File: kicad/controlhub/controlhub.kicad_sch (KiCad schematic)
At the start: 0 parts

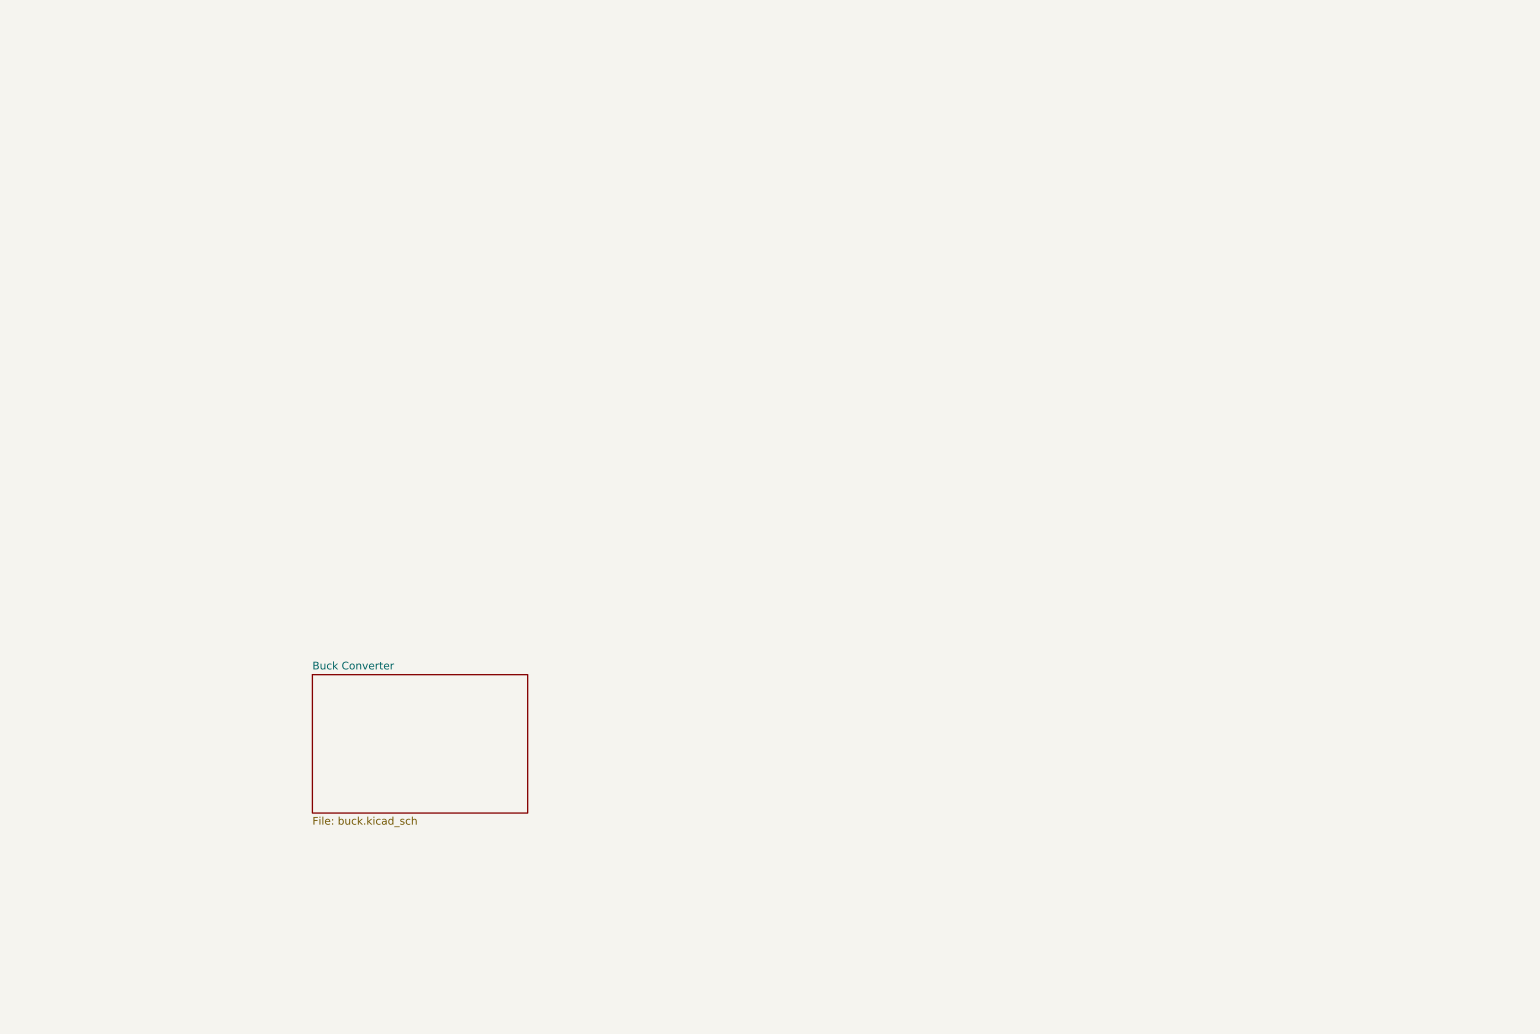
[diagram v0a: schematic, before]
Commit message: added converter and started servo driver
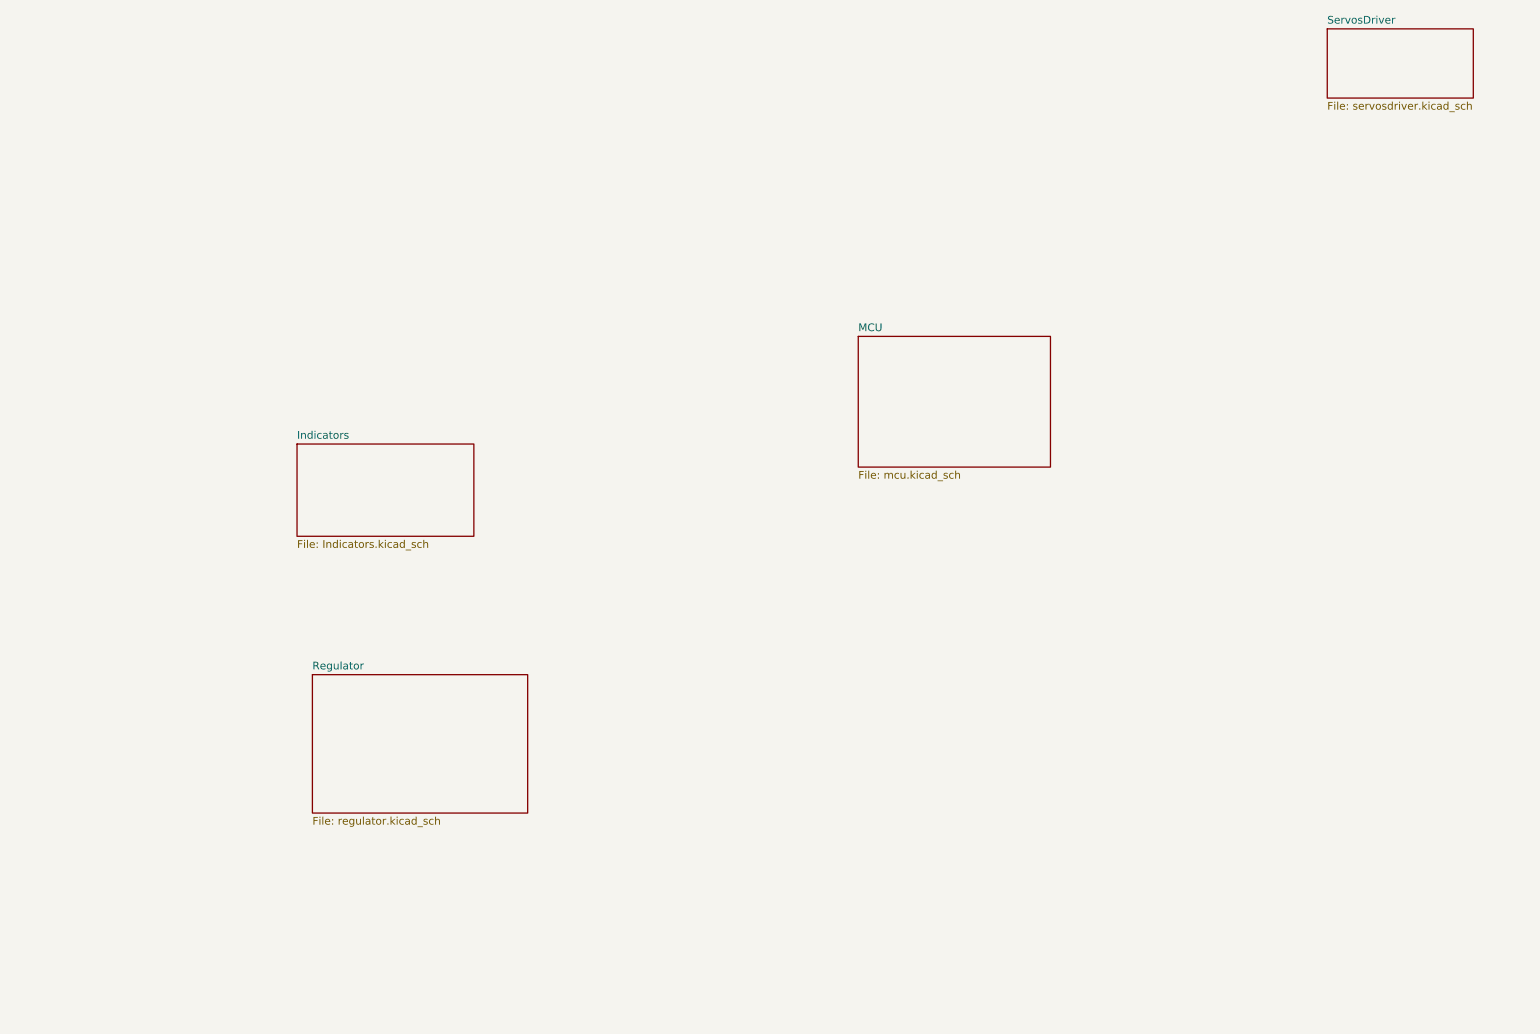
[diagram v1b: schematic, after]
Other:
- sheet Buck Converter renamed Regulator
- added sheet Indicators (Indicators.kicad_sch)
- added sheet MCU (mcu.kicad_sch)
- added sheet ServosDriver (servosdriver.kicad_sch)
- sheet Regulator: file buck.kicad_sch -> regulator.kicad_sch
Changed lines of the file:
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@@
+	)
+	(sheet
+		(at 63.5 102.87)
+		(size 29.21 15.24)
+		(exclude_from_sim no)
+		(in_bom yes)
+		(on_board yes)
+		(dnp no)
+		(fields_autoplaced yes)
+		(stroke
+			(width 0.1524)
+			(type solid)
+		)
+		(fill
+			(color 0 0 0 0.0000)
+		)
+		(property "Sheetname" "Indicators"
+			(at 63.5 102.1584 0)
+			(effects
+				(font
+					(size 1.27 1.27)
+				)
+				(justify left bottom)
+			)
+		)
+		(property "Sheetfile" "Indicators.kicad_sch"
+			(at 63.5 118.6946 0)
+			(effects
+				(font
+					(size 1.27 1.27)
+				)
+				(justify left top)
+			)
+		)
+		(instances
+			(project "controlhub"
+				(path "/78f9b8b9-94ed-46bb-ab2b-797c156bf665"
+					(page "3")
+				)
+			)
+		)
+	)
+	(sheet
+		(at 156.21 85.09)
+		(size 31.75 21.59)
+		(exclude_from_sim no)
+		(in_bom yes)
+		(on_board yes)
+		(dnp no)
+		(fields_autoplaced yes)
+		(stroke
+			(width 0.1524)
+			(type solid)
+		)
+		(fill
+			(color 0 0 0 0.0000)
+		)
+		(property "Sheetname" "MCU"
+			(at 156.21 84.3784 0)
+			(effects
+				(font
+					(size 1.27 1.27)
+				)
+				(justify left bottom)
+			)
+		)
+		(property "Sheetfile" "mcu.kicad_sch"
+			(at 156.21 107.2646 0)
+			(effects
+				(font
+					(size 1.27 1.27)
+				)
+				(justify left top)
+			)
+		)
+		(instances
+			(project "controlhub"
+				(path "/78f9b8b9-94ed-46bb-ab2b-797c156bf665"
+					(page "4")
+				)
+			)
+		)
 	)
 	(sheet
@@
 			(color 0 0 0 0.0000)
 		)
-		(property "Sheetname" "Buck Converter"
+		(property "Sheetname" "Regulator"
 			(at 66.04 140.2584 0)
 			(effects
@@
 			)
 		)
-		(property "Sheetfile" "buck.kicad_sch"
+		(property "Sheetfile" "regulator.kicad_sch"
 			(at 66.04 164.4146 0)
 			(effects
@@
 				)
 			)
+		)
+	)
+	(sheet
+		(at 233.68 34.29)
+		(size 24.13 11.43)
+		(exclude_from_sim no)
+		(in_bom yes)
+		(on_board yes)
+		(dnp no)
+		(fields_autoplaced yes)
+		(stroke
+			(width 0.1524)
+			(type solid)
+		)
+		(fill
+			(color 0 0 0 0.0000)
+		)
+		(property "Sheetname" "ServosDriver"
+			(at 233.68 33.5784 0)
+			(effects
+				(font
+					(size 1.27 1.27)
+				)
+				(justify left bottom)
+			)
+		)
+		(property "Sheetfile" "servosdriver.kicad_sch"
+			(at 233.68 46.3046 0)
+			(effects
+				(font
+					(size 1.27 1.27)
+				)
+				(justify left top)
+			)
+		)
+		(instances
+			(project "controlhub"
+				(path "/78f9b8b9-94ed-46bb-ab2b-797c156bf665"
+					(page "5")
+				)
+			)

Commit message: added driver
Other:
- added sheet MotorDriver (motordriver.kicad_sch)
- added sheet MotorDriver1 (motordriver.kicad_sch)
- added sheet MotorDriver2 (motordriver.kicad_sch)
- added sheet MotorDriver3 (motordriver.kicad_sch)
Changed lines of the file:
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@@
+	)
+	(sheet
+		(at 77.47 41.91)
+		(size 26.67 15.24)
+		(exclude_from_sim no)
+		(in_bom yes)
+		(on_board yes)
+		(dnp no)
+		(fields_autoplaced yes)
+		(stroke
+			(width 0.1524)
+			(type solid)
+		)
+		(fill
+			(color 0 0 0 0.0000)
+		)
+		(property "Sheetname" "MotorDriver"
+			(at 77.47 41.1984 0)
+			(effects
+				(font
+					(size 1.27 1.27)
+				)
+				(justify left bottom)
+			)
+		)
+		(property "Sheetfile" "motordriver.kicad_sch"
+			(at 77.47 57.7346 0)
+			(effects
+				(font
+					(size 1.27 1.27)
+				)
+				(justify left top)
+			)
+		)
+		(instances
+			(project "controlhub"
+				(path "/78f9b8b9-94ed-46bb-ab2b-797c156bf665"
+					(page "6")
+				)
+			)
+		)
 	)
 	(sheet
@@
 	)
 	(sheet
-		(at 66.04 140.97)
-		(size 35.56 22.86)
+		(at 36.83 62.23)
+		(size 26.67 15.24)
+		(exclude_from_sim no)
+		(in_bom yes)
+		(on_board yes)
+		(dnp no)
+		(fields_autoplaced yes)
+		(stroke
+			(width 0.1524)
+			(type solid)
+		)
+		(fill
+			(color 0 0 0 0.0000)
+		)
+		(property "Sheetname" "MotorDriver2"
+			(at 36.83 61.5184 0)
+			(effects
+				(font
+					(size 1.27 1.27)
+				)
+				(justify left bottom)
+			)
+		)
+		(property "Sheetfile" "motordriver.kicad_sch"
+			(at 36.83 78.0546 0)
+			(effects
+				(font
+					(size 1.27 1.27)
+				)
+				(justify left top)
+			)
+		)
+		(instances
+			(project "controlhub"
+				(path "/78f9b8b9-94ed-46bb-ab2b-797c156bf665"
+					(page "8")
+				)
+			)
+		)
+	)
+	(sheet
+		(at 16.51 186.69)
+		(size 13.97 8.89)
 		(exclude_from_sim no)
 		(in_bom yes)
@@
 		)
 		(property "Sheetname" "Regulator"
-			(at 66.04 140.2584 0)
+			(at 16.51 185.9784 0)
 			(effects
 				(font
@@
 		)
 		(property "Sheetfile" "regulator.kicad_sch"
-			(at 66.04 164.4146 0)
+			(at 16.51 196.1646 0)
 			(effects
 				(font
@@
 				(path "/78f9b8b9-94ed-46bb-ab2b-797c156bf665"
 					(page "2")
+				)
+			)
+		)
+	)
+	(sheet
+		(at 36.83 39.37)
+		(size 26.67 15.24)
+		(exclude_from_sim no)
+		(in_bom yes)
+		(on_board yes)
+		(dnp no)
+		(fields_autoplaced yes)
+		(stroke
+			(width 0.1524)
+			(type solid)
+		)
+		(fill
+			(color 0 0 0 0.0000)
+		)
+		(property "Sheetname" "MotorDriver1"
+			(at 36.83 38.6584 0)
+			(effects
+				(font
+					(size 1.27 1.27)
+				)
+				(justify left bottom)
+			)
+		)
+		(property "Sheetfile" "motordriver.kicad_sch"
+			(at 36.83 55.1946 0)
+			(effects
+				(font
+					(size 1.27 1.27)
+				)
+				(justify left top)
+			)
+		)
+		(instances
+			(project "controlhub"
+				(path "/78f9b8b9-94ed-46bb-ab2b-797c156bf665"
+					(page "7")
 				)
 			)
@@
 				)
 			)
+		)
+	)
+	(sheet
+		(at 77.47 63.5)
+		(size 26.67 15.24)
+		(exclude_from_sim no)
+		(in_bom yes)
+		(on_board yes)
+		(dnp no)
+		(fields_autoplaced yes)
+		(stroke
+			(width 0.1524)
+			(type solid)
+		)
+		(fill
+			(color 0 0 0 0.0000)
+		)
+		(property "Sheetname" "MotorDriver3"
+			(at 77.47 62.7884 0)
+			(effects
+				(font
+					(size 1.27 1.27)
+				)
+				(justify left bottom)
+			)
+		)
+		(property "Sheetfile" "motordriver.kicad_sch"
+			(at 77.47 79.3246 0)
+			(effects
+				(font
+					(size 1.27 1.27)
+				)
+				(justify left top)
+			)
+		)
+		(instances
+			(project "controlhub"
+				(path "/78f9b8b9-94ed-46bb-ab2b-797c156bf665"
+					(page "9")
+				)
+			)
